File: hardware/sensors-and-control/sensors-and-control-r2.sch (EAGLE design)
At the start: 133 parts, among them IC1 STM32L496ZET6

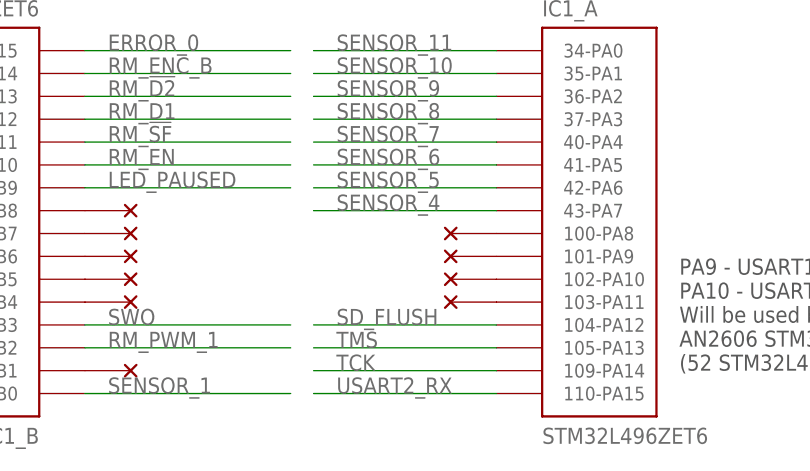
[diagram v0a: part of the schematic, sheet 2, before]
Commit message: - added a bit of SPI initialization code - moved SD flush to A12 with it's own EXTI - added 2nd revision board (see revision-history.txt for details)
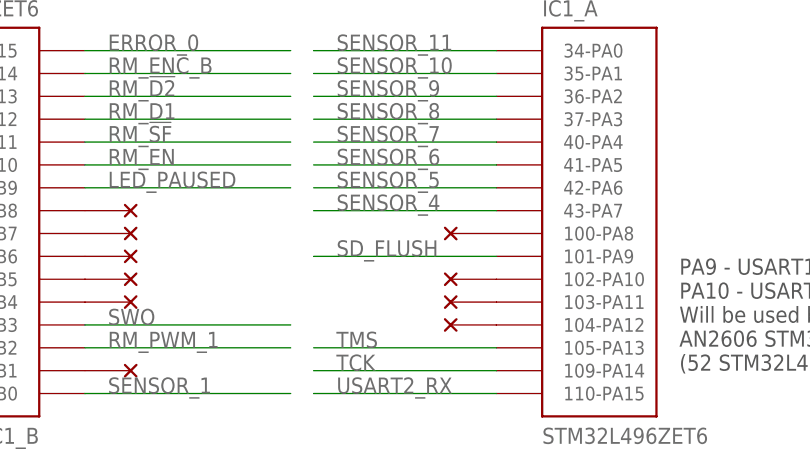
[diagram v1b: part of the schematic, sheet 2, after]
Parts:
- removed U$30: NC, voltage-ground:NC
- added U$19: NC, voltage-ground:NC
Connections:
- removed net N$46: IC1_A.101-PA9, U$30.1
- new net N$35: IC1_A.104-PA12, U$19.1
- net SD_FLUSH: now also IC1_A.101-PA9; no longer IC1_A.104-PA12
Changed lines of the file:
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@@
 <part name="U$14" library="voltage-ground" library_urn="urn:adsk.eagle:library:704746" deviceset="NC" device=""/>
 <part name="U$29" library="voltage-ground" library_urn="urn:adsk.eagle:library:704746" deviceset="NC" device=""/>
-<part name="U$30" library="voltage-ground" library_urn="urn:adsk.eagle:library:704746" deviceset="NC" device=""/>
 <part name="U$37" library="voltage-ground" library_urn="urn:adsk.eagle:library:704746" deviceset="NC" device=""/>
 <part name="U$17" library="voltage-ground" library_urn="urn:adsk.eagle:library:704746" deviceset="NC" device=""/>
 <part name="U$18" library="voltage-ground" library_urn="urn:adsk.eagle:library:704746" deviceset="NC" device=""/>
+<part name="U$19" library="voltage-ground" library_urn="urn:adsk.eagle:library:704746" deviceset="NC" device=""/>
 </parts>
 <sheets>
@@
 <instance part="U$14" gate="G$1" x="73.66" y="30.48" rot="R180"/>
 <instance part="U$29" gate="G$1" x="129.54" y="165.1"/>
-<instance part="U$30" gate="G$1" x="73.66" y="35.56" rot="R180"/>
 <instance part="U$37" gate="G$1" x="73.66" y="33.02" rot="R180"/>
 <instance part="U$17" gate="G$1" x="129.54" y="142.24"/>
 <instance part="U$18" gate="G$1" x="129.54" y="139.7"/>
+<instance part="U$19" gate="G$1" x="73.66" y="27.94" rot="R180"/>
 </instances>
 <busses>
@@
 </segment>
 </net>
-<net name="SD_FLUSH" class="0">
-<segment>
-<pinref part="IC1" gate="_A" pin="104-PA12"/>
-<wire x1="76.2" y1="27.94" x2="55.88" y2="27.94" width="0.1524" layer="91"/>
-<label x="58.42" y="27.94" size="1.778" layer="95"/>
-</segment>
-</net>
 <net name="N$30" class="0">
 <segment>
@@
 <pinref part="IC1" gate="_G" pin="132-PG15"/>
 <pinref part="U$29" gate="G$1" pin="1"/>
-</segment>
-</net>
-<net name="N$46" class="0">
-<segment>
-<pinref part="IC1" gate="_A" pin="101-PA9"/>
-<pinref part="U$30" gate="G$1" pin="1"/>
 </segment>
 </net>
@@
 </segment>
 </net>
+<net name="SD_FLUSH" class="0">
+<segment>
+<pinref part="IC1" gate="_A" pin="101-PA9"/>
+<wire x1="76.2" y1="35.56" x2="55.88" y2="35.56" width="0.1524" layer="91"/>
+<label x="58.42" y="35.56" size="1.778" layer="95"/>
+</segment>
+</net>
+<net name="N$35" class="0">
+<segment>
+<pinref part="IC1" gate="_A" pin="104-PA12"/>
+<pinref part="U$19" gate="G$1" pin="1"/>
+</segment>
+</net>

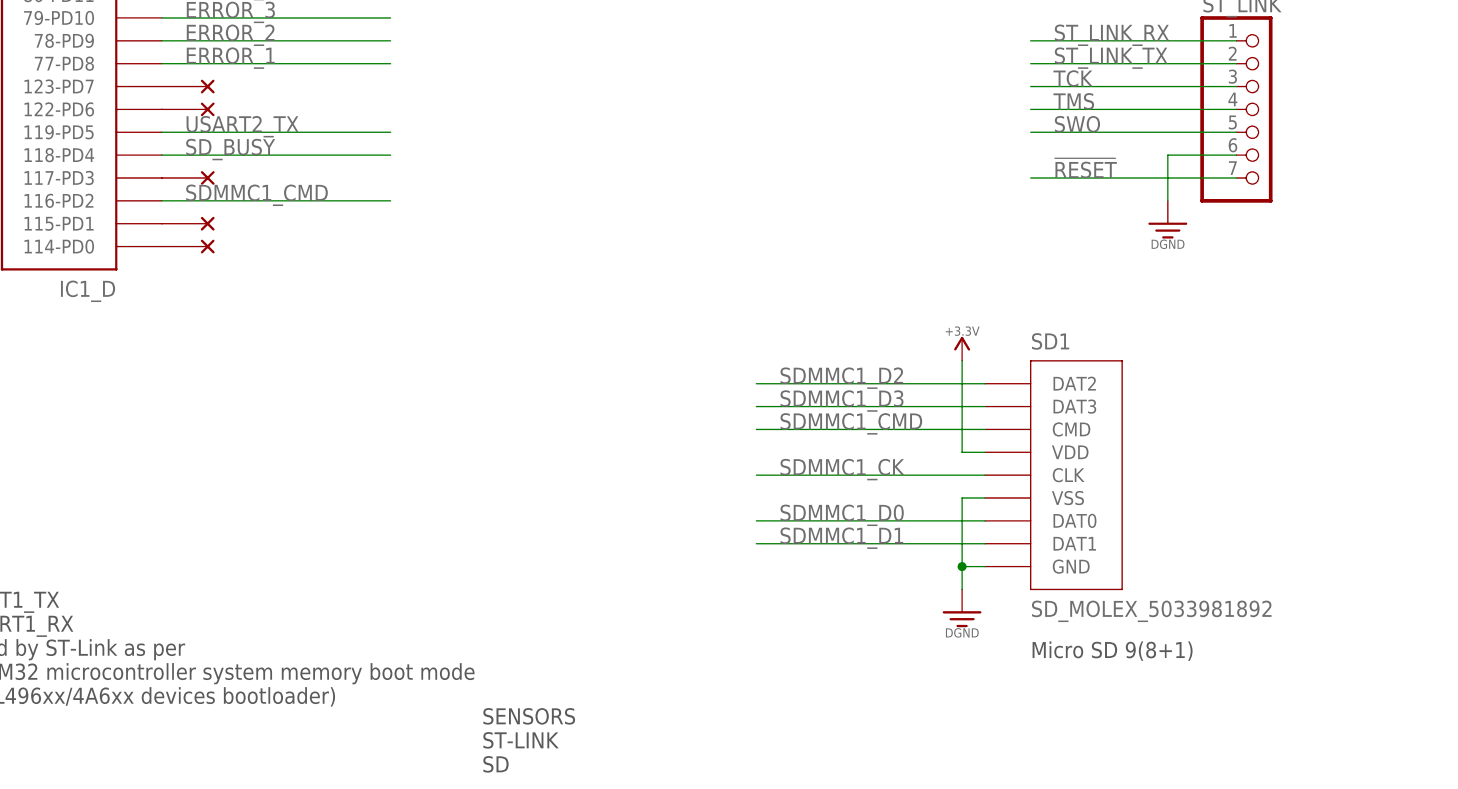
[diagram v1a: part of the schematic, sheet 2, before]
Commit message: - added SD card detection PIN (D1) - added pullup resistors for SD's D0-D3 and CMD lines (47k)
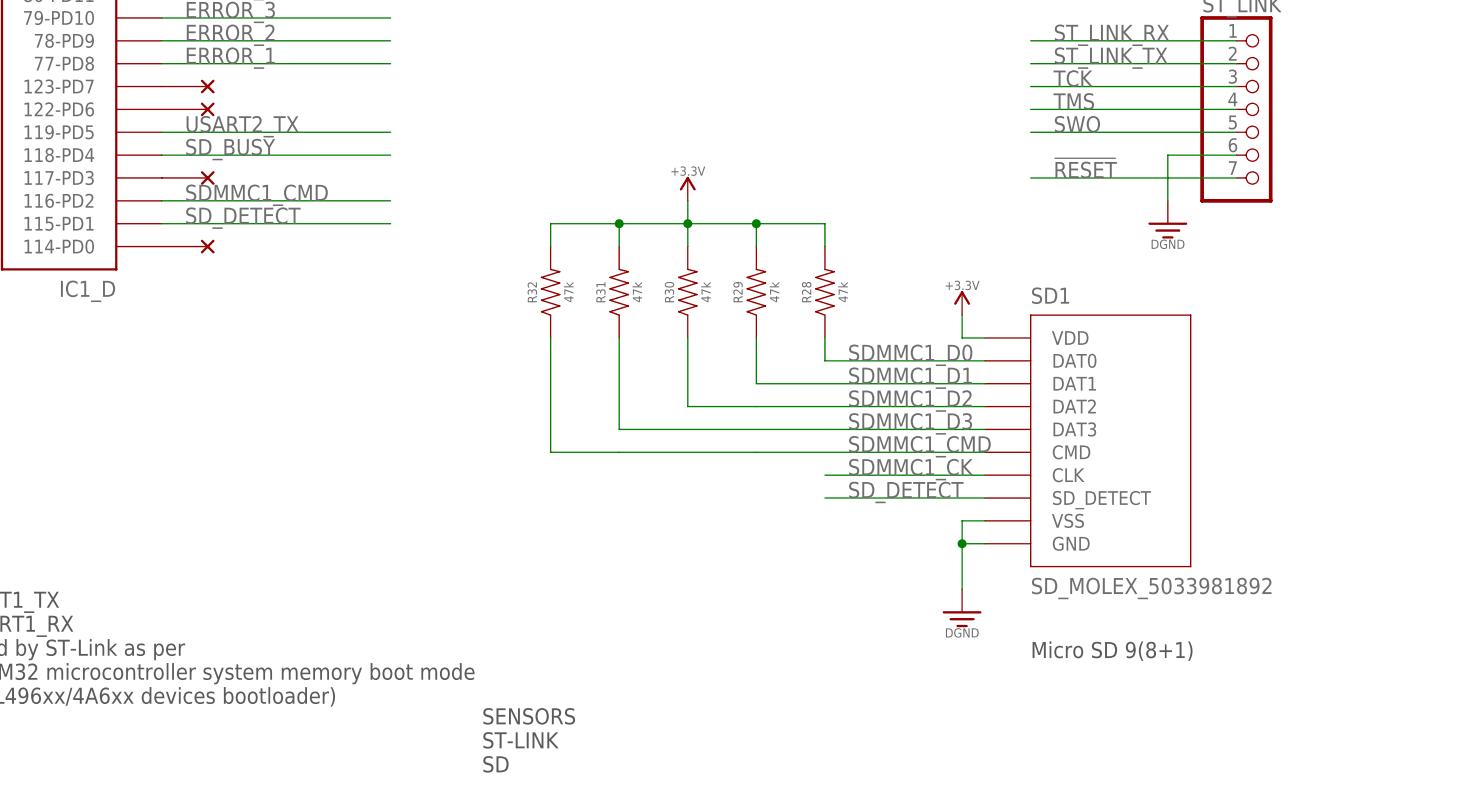
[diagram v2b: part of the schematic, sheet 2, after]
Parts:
- removed U$12: NC, voltage-ground:NC
- added R28, R29, R30, R31, R32: 47k, resistors:RESISTOR_0.1W
- added SUPPLY14: +3.3V, voltage-ground:+3.3V
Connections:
- removed net N$28: IC1_D.115-PD1, U$12.1
- new net SD_DETECT: IC1_D.115-PD1, SD1.SD_DETECT
- net SDMMC1_CMD: now also R32.1
- net SDMMC1_D0: now also R28.1
- net SDMMC1_D1: now also R29.1
- net SDMMC1_D2: now also R30.1
- net SDMMC1_D3: now also R31.1
- net VDD: now also R28.2, R29.2, R30.2, R31.2, R32.2, SUPPLY14.VCC
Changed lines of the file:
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@@
 <part name="U$10" library="voltage-ground" library_urn="urn:adsk.eagle:library:704746" deviceset="NC" device=""/>
 <part name="U$11" library="voltage-ground" library_urn="urn:adsk.eagle:library:704746" deviceset="NC" device=""/>
-<part name="U$12" library="voltage-ground" library_urn="urn:adsk.eagle:library:704746" deviceset="NC" device=""/>
 <part name="U$13" library="voltage-ground" library_urn="urn:adsk.eagle:library:704746" deviceset="NC" device=""/>
 <part name="U$15" library="voltage-ground" library_urn="urn:adsk.eagle:library:704746" deviceset="NC" device=""/>
@@
 <part name="U$18" library="voltage-ground" library_urn="urn:adsk.eagle:library:704746" deviceset="NC" device=""/>
 <part name="U$19" library="voltage-ground" library_urn="urn:adsk.eagle:library:704746" deviceset="NC" device=""/>
+<part name="R28" library="resistors" library_urn="urn:adsk.eagle:library:704770" deviceset="RESISTOR_0.1W" device="" package3d_urn="urn:adsk.eagle:package:704947/3" value="47k"/>
+<part name="R29" library="resistors" library_urn="urn:adsk.eagle:library:704770" deviceset="RESISTOR_0.1W" device="" package3d_urn="urn:adsk.eagle:package:704947/3" value="47k"/>
+<part name="R30" library="resistors" library_urn="urn:adsk.eagle:library:704770" deviceset="RESISTOR_0.1W" device="" package3d_urn="urn:adsk.eagle:package:704947/3" value="47k"/>
+<part name="R31" library="resistors" library_urn="urn:adsk.eagle:library:704770" deviceset="RESISTOR_0.1W" device="" package3d_urn="urn:adsk.eagle:package:704947/3" value="47k"/>
+<part name="R32" library="resistors" library_urn="urn:adsk.eagle:library:704770" deviceset="RESISTOR_0.1W" device="" package3d_urn="urn:adsk.eagle:package:704947/3" value="47k"/>
+<part name="SUPPLY14" library="voltage-ground" library_urn="urn:adsk.eagle:library:704746" deviceset="+3.3V" device=""/>
 </parts>
 <sheets>
@@
 <instance part="SD1" gate="G$1" x="223.52" y="38.1"/>
 <instance part="DGND29" gate="G$2" x="215.9" y="33.02"/>
-<instance part="SUPPLY9" gate="G$1" x="215.9" y="60.96"/>
+<instance part="SUPPLY9" gate="G$1" x="215.9" y="66.04"/>
 <instance part="IC1" gate="_D" x="121.92" y="114.3" rot="R180"/>
 <instance part="U$11" gate="G$1" x="129.54" y="73.66"/>
-<instance part="U$12" gate="G$1" x="129.54" y="76.2"/>
 <instance part="U$13" gate="G$1" x="129.54" y="81.28"/>
 <instance part="U$15" gate="G$1" x="129.54" y="88.9"/>
@@
 <instance part="U$18" gate="G$1" x="129.54" y="139.7"/>
 <instance part="U$19" gate="G$1" x="73.66" y="27.94" rot="R180"/>
+<instance part="R28" gate="G$1" x="200.66" y="68.58" rot="R90"/>
+<instance part="R29" gate="G$1" x="193.04" y="68.58" rot="R90"/>
+<instance part="R30" gate="G$1" x="185.42" y="68.58" rot="R90"/>
+<instance part="R31" gate="G$1" x="177.8" y="68.58" rot="R90"/>
+<instance part="R32" gate="G$1" x="170.18" y="68.58" rot="R90"/>
+<instance part="SUPPLY14" gate="G$1" x="185.42" y="78.74"/>
 </instances>
 <busses>
@@
 <segment>
 <pinref part="DGND29" gate="G$2" pin="DGND"/>
-<wire x1="215.9" y1="35.56" x2="215.9" y2="38.1" width="0.1524" layer="91"/>
+<wire x1="215.9" y1="35.56" x2="215.9" y2="40.64" width="0.1524" layer="91"/>
 <pinref part="SD1" gate="G$1" pin="VSS"/>
-<wire x1="215.9" y1="38.1" x2="215.9" y2="45.72" width="0.1524" layer="91"/>
-<wire x1="215.9" y1="45.72" x2="218.44" y2="45.72" width="0.1524" layer="91"/>
-<junction x="215.9" y="38.1"/>
+<wire x1="215.9" y1="40.64" x2="215.9" y2="43.18" width="0.1524" layer="91"/>
+<wire x1="215.9" y1="43.18" x2="218.44" y2="43.18" width="0.1524" layer="91"/>
+<junction x="215.9" y="40.64"/>
 <pinref part="SD1" gate="G$1" pin="GND"/>
-<wire x1="218.44" y1="38.1" x2="215.9" y2="38.1" width="0.1524" layer="91"/>
+<wire x1="218.44" y1="40.64" x2="215.9" y2="40.64" width="0.1524" layer="91"/>
 </segment>
 </net>
@@
 <segment>
 <pinref part="SD1" gate="G$1" pin="VDD"/>
-<wire x1="218.44" y1="50.8" x2="215.9" y2="50.8" width="0.1524" layer="91"/>
+<wire x1="218.44" y1="63.5" x2="215.9" y2="63.5" width="0.1524" layer="91"/>
 <pinref part="SUPPLY9" gate="G$1" pin="VCC"/>
-<wire x1="215.9" y1="50.8" x2="215.9" y2="60.96" width="0.1524" layer="91"/>
+<wire x1="215.9" y1="63.5" x2="215.9" y2="66.04" width="0.1524" layer="91"/>
 </segment>
 <segment>
@@
 <wire x1="25.4" y1="149.86" x2="30.48" y2="149.86" width="0.1524" layer="91"/>
 </segment>
+<segment>
+<pinref part="R32" gate="G$1" pin="2"/>
+<wire x1="170.18" y1="73.66" x2="170.18" y2="76.2" width="0.1524" layer="91"/>
+<wire x1="170.18" y1="76.2" x2="177.8" y2="76.2" width="0.1524" layer="91"/>
+<pinref part="R28" gate="G$1" pin="2"/>
+<wire x1="177.8" y1="76.2" x2="185.42" y2="76.2" width="0.1524" layer="91"/>
+<wire x1="185.42" y1="76.2" x2="193.04" y2="76.2" width="0.1524" layer="91"/>
+<wire x1="193.04" y1="76.2" x2="200.66" y2="76.2" width="0.1524" layer="91"/>
+<wire x1="200.66" y1="76.2" x2="200.66" y2="73.66" width="0.1524" layer="91"/>
+<junction x="177.8" y="76.2"/>
+<junction x="185.42" y="76.2"/>
+<junction x="193.04" y="76.2"/>
+<pinref part="SUPPLY14" gate="G$1" pin="VCC"/>
+<wire x1="185.42" y1="78.74" x2="185.42" y2="76.2" width="0.1524" layer="91"/>
+<pinref part="R29" gate="G$1" pin="2"/>
+<wire x1="193.04" y1="76.2" x2="193.04" y2="73.66" width="0.1524" layer="91"/>
+<pinref part="R30" gate="G$1" pin="2"/>
+<wire x1="185.42" y1="76.2" x2="185.42" y2="73.66" width="0.1524" layer="91"/>
+<pinref part="R31" gate="G$1" pin="2"/>
+<wire x1="177.8" y1="76.2" x2="177.8" y2="73.66" width="0.1524" layer="91"/>
+</segment>
 </net>
 <net name="N$2" class="0">
@@
 <net name="SDMMC1_D0" class="0">
 <segment>
-<pinref part="SD1" gate="G$1" pin="DAT0"/>
-<wire x1="218.44" y1="43.18" x2="193.04" y2="43.18" width="0.1524" layer="91"/>
-<label x="195.58" y="43.18" size="1.778" layer="95"/>
-</segment>
-<segment>
 <pinref part="IC1" gate="_C" pin="98-PC8"/>
 <wire x1="76.2" y1="91.44" x2="55.88" y2="91.44" width="0.1524" layer="91"/>
 <label x="58.42" y="91.44" size="1.778" layer="95"/>
 </segment>
+<segment>
+<pinref part="SD1" gate="G$1" pin="DAT0"/>
+<wire x1="218.44" y1="60.96" x2="200.66" y2="60.96" width="0.1524" layer="91"/>
+<label x="203.2" y="60.96" size="1.778" layer="95"/>
+<pinref part="R28" gate="G$1" pin="1"/>
+<wire x1="200.66" y1="60.96" x2="200.66" y2="63.5" width="0.1524" layer="91"/>
+</segment>
 </net>
 <net name="SDMMC1_D1" class="0">
 <segment>
 <pinref part="SD1" gate="G$1" pin="DAT1"/>
-<wire x1="218.44" y1="40.64" x2="193.04" y2="40.64" width="0.1524" layer="91"/>
-<label x="195.58" y="40.64" size="1.778" layer="95"/>
+<wire x1="218.44" y1="58.42" x2="193.04" y2="58.42" width="0.1524" layer="91"/>
+<label x="203.2" y="58.42" size="1.778" layer="95"/>
+<pinref part="R29" gate="G$1" pin="1"/>
+<wire x1="193.04" y1="63.5" x2="193.04" y2="58.42" width="0.1524" layer="91"/>
 </segment>
 <segment>
@@
 <segment>
 <pinref part="SD1" gate="G$1" pin="DAT2"/>
-<wire x1="218.44" y1="58.42" x2="193.04" y2="58.42" width="0.1524" layer="91"/>
-<label x="195.58" y="58.42" size="1.778" layer="95"/>
+<wire x1="218.44" y1="55.88" x2="193.04" y2="55.88" width="0.1524" layer="91"/>
+<label x="203.2" y="55.88" size="1.778" layer="95"/>
+<wire x1="193.04" y1="55.88" x2="185.42" y2="55.88" width="0.1524" layer="91"/>
+<pinref part="R30" gate="G$1" pin="1"/>
+<wire x1="185.42" y1="55.88" x2="185.42" y2="63.5" width="0.1524" layer="91"/>
 </segment>
 <segment>
@@
 <segment>
 <pinref part="SD1" gate="G$1" pin="DAT3"/>
-<wire x1="218.44" y1="55.88" x2="193.04" y2="55.88" width="0.1524" layer="91"/>
-<label x="195.58" y="55.88" size="1.778" layer="95"/>
+<wire x1="218.44" y1="53.34" x2="200.66" y2="53.34" width="0.1524" layer="91"/>
+<label x="203.2" y="53.34" size="1.778" layer="95"/>
+<wire x1="200.66" y1="53.34" x2="177.8" y2="53.34" width="0.1524" layer="91"/>
+<pinref part="R31" gate="G$1" pin="1"/>
+<wire x1="177.8" y1="53.34" x2="177.8" y2="63.5" width="0.1524" layer="91"/>
 </segment>
 <segment>
@@
 <segment>
 <pinref part="SD1" gate="G$1" pin="CLK"/>
-<wire x1="218.44" y1="48.26" x2="193.04" y2="48.26" width="0.1524" layer="91"/>
-<label x="195.58" y="48.26" size="1.778" layer="95"/>
+<wire x1="218.44" y1="48.26" x2="200.66" y2="48.26" width="0.1524" layer="91"/>
+<label x="203.2" y="48.26" size="1.778" layer="95"/>
 </segment>
 <segment>
@@
 <segment>
 <pinref part="SD1" gate="G$1" pin="CMD"/>
-<wire x1="218.44" y1="53.34" x2="193.04" y2="53.34" width="0.1524" layer="91"/>
-<label x="195.58" y="53.34" size="1.778" layer="95"/>
+<wire x1="218.44" y1="50.8" x2="193.04" y2="50.8" width="0.1524" layer="91"/>
+<label x="203.2" y="50.8" size="1.778" layer="95"/>
+<wire x1="193.04" y1="50.8" x2="177.8" y2="50.8" width="0.1524" layer="91"/>
+<wire x1="177.8" y1="50.8" x2="170.18" y2="50.8" width="0.1524" layer="91"/>
+<pinref part="R32" gate="G$1" pin="1"/>
+<wire x1="170.18" y1="50.8" x2="170.18" y2="63.5" width="0.1524" layer="91"/>
 </segment>
 <segment>
@@
 </segment>
 </net>
-<net name="N$28" class="0">
-<segment>
-<pinref part="IC1" gate="_D" pin="115-PD1"/>
-<pinref part="U$12" gate="G$1" pin="1"/>
-</segment>
-</net>
 <net name="N$29" class="0">
 <segment>
@@
 </segment>
 </net>
+<net name="SD_DETECT" class="0">
+<segment>
+<pinref part="SD1" gate="G$1" pin="SD_DETECT"/>
+<wire x1="218.44" y1="45.72" x2="200.66" y2="45.72" width="0.1524" layer="91"/>
+<label x="203.2" y="45.72" size="1.778" layer="95"/>
+</segment>
+<segment>
+<pinref part="IC1" gate="_D" pin="115-PD1"/>
+<wire x1="127" y1="76.2" x2="152.4" y2="76.2" width="0.1524" layer="91"/>
+<label x="129.54" y="76.2" size="1.778" layer="95"/>
+</segment>
+</net>
